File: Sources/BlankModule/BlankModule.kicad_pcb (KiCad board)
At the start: 2 copper layers, 31 x 22 mm, 2 parts

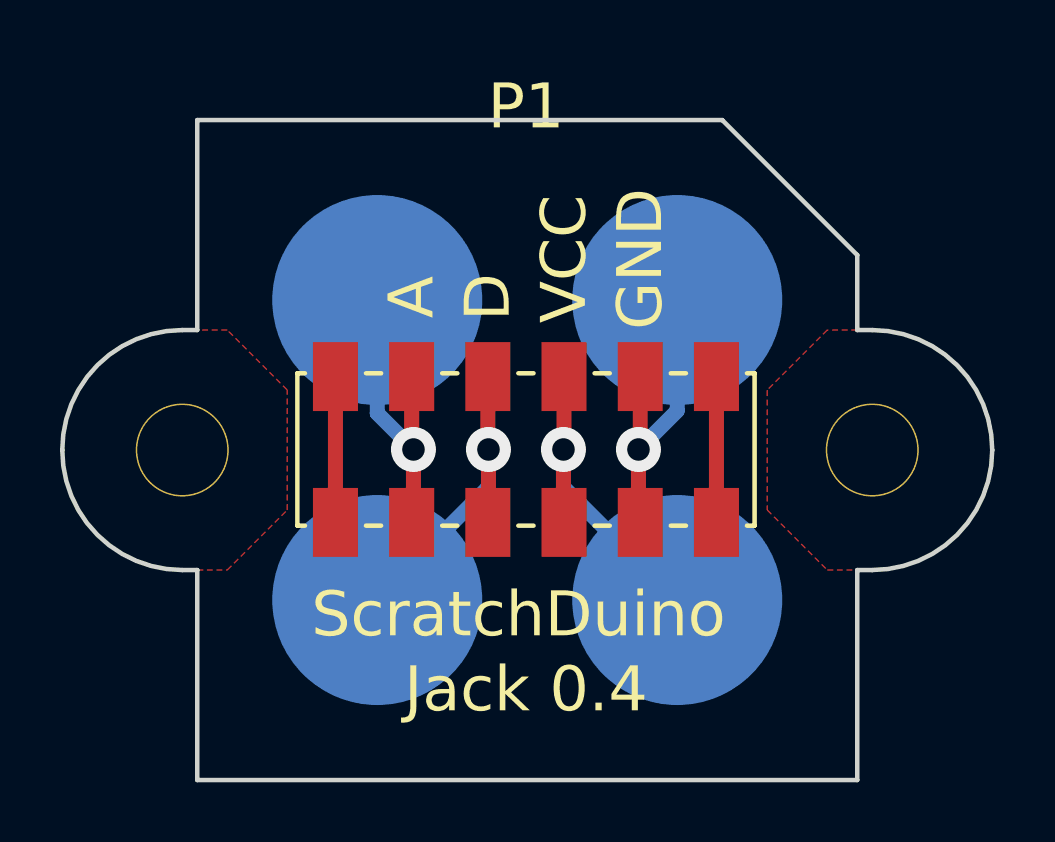
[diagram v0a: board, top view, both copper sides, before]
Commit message: Body has been added
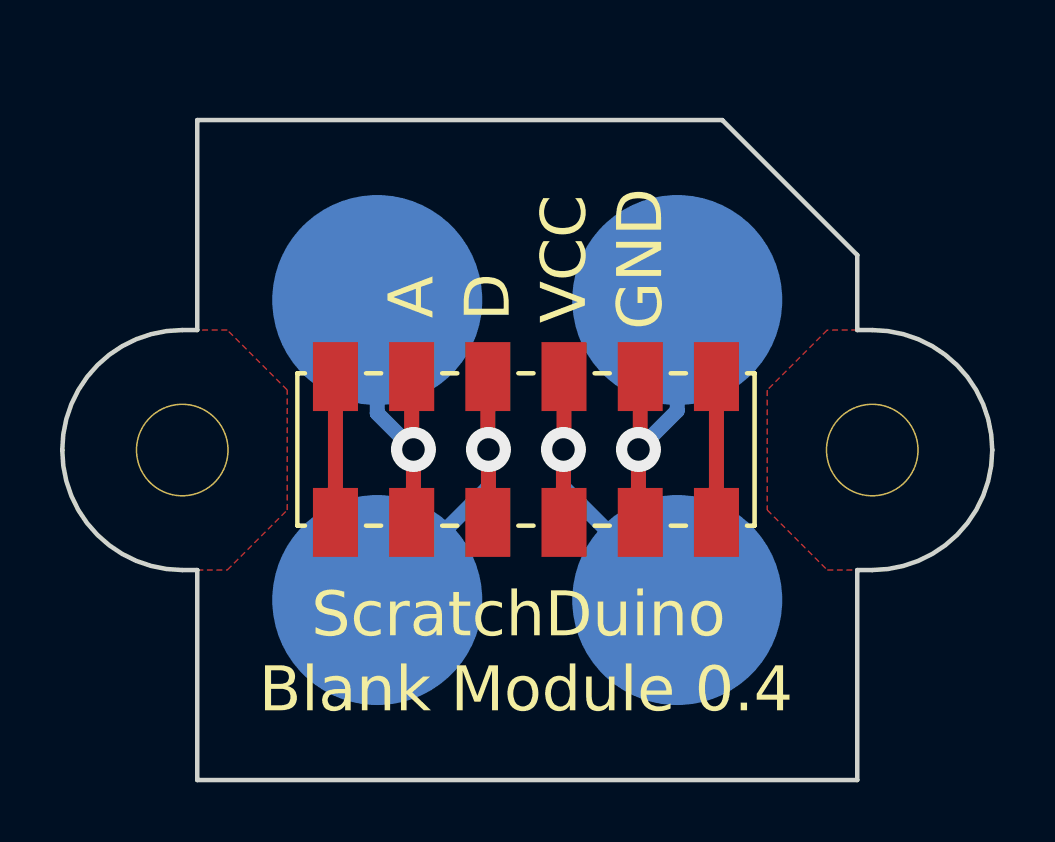
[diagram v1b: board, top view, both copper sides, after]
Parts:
- renumbered P1 to ?
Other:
- board text added: "Blank Module 0.4"
- board text removed: "Jack 0.4"
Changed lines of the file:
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@@
   (layers
     (15 F.Cu signal)
-    (0 B.Cu signal)
+    (0 B.Cu signal hide)
     (16 B.Adhes user hide)
     (17 F.Adhes user hide)
-    (18 B.Paste user)
-    (19 F.Paste user)
-    (20 B.SilkS user)
+    (18 B.Paste user hide)
+    (19 F.Paste user hide)
+    (20 B.SilkS user hide)
     (21 F.SilkS user)
     (22 B.Mask user hide)
-    (23 F.Mask user)
+    (23 F.Mask user hide)
     (24 Dwgs.User user hide)
     (25 Cmts.User user hide)
@@
   (module SENSOR_JACK (layer F.Cu)
     (at 29.25 25.75)
-    (fp_text reference P1 (at 0 -11.43) (layer F.SilkS)
+    (fp_text reference "" (at 0 -11.43) (layer F.SilkS)
       (effects (font (size 1.5 1.5) (thickness 0.15)))
     )
@@
     )
   )
-  (gr_text "Jack 0.4" (at 29.25 33.75) (layer F.SilkS)
+  (gr_text "Blank Module 0.4" (at 29.25 33.75) (layer F.SilkS)
     (effects (font (size 1.5 1.5) (thickness 0.3)))
   )
@@
   (via (at 33 25.75) (size 1.5) (layers F.Cu B.Cu) (net 1))
   (segment (start 34.293 24.457) (end 33 25.75) (width 0.5) (layer B.Cu) (net 1))
-  (segment (start 35.6 23.32) (end 35.6 28.18) (width 0.5) (layer F.Cu) (net 2) (status C00000))
-  (segment (start 22.9 23.32) (end 22.9 28.18) (width 0.5) (layer F.Cu) (net 3) (status C00000))
-  (segment (start 30.5 25.75) (end 30.5 28.16) (width 0.5) (layer F.Cu) (net 4) (status 800000))
-  (segment (start 30.5 28.16) (end 30.52 28.18) (width 0.5) (layer F.Cu) (net 4) (status C00000))
-  (segment (start 30.52 23.32) (end 30.52 25.73) (width 0.5) (layer F.Cu) (net 4) (status 400000))
-  (segment (start 34.269 30.769) (end 34.293 30.769) (width 0.5) (layer B.Cu) (net 4) (status C00000))
-  (segment (start 30.5 27) (end 34.269 30.769) (width 0.5) (layer B.Cu) (net 4) (status 800000))
+  (segment (start 35.6 23.32) (end 35.6 28.18) (width 0.5) (layer F.Cu) (net 2))
+  (segment (start 22.9 23.32) (end 22.9 28.18) (width 0.5) (layer F.Cu) (net 3))
+  (segment (start 30.5 25.75) (end 30.5 28.16) (width 0.5) (layer F.Cu) (net 4))
+  (segment (start 30.5 28.16) (end 30.52 28.18) (width 0.5) (layer F.Cu) (net 4))
+  (segment (start 30.52 23.32) (end 30.52 25.73) (width 0.5) (layer F.Cu) (net 4))
+  (segment (start 34.269 30.769) (end 34.293 30.769) (width 0.5) (layer B.Cu) (net 4))
+  (segment (start 30.5 27) (end 34.269 30.769) (width 0.5) (layer B.Cu) (net 4))
   (segment (start 30.5 25.75) (end 30.5 27) (width 0.5) (layer B.Cu) (net 4))
   (via (at 30.5 25.75) (size 1.5) (layers F.Cu B.Cu) (net 4))
   (segment (start 30.52 25.73) (end 30.5 25.75) (width 0.5) (layer F.Cu) (net 4))
-  (segment (start 28 25.75) (end 28 28.16) (width 0.5) (layer F.Cu) (net 5) (status 800000))
-  (segment (start 28 28.16) (end 27.98 28.18) (width 0.5) (layer F.Cu) (net 5) (status C00000))
-  (segment (start 27.98 23.32) (end 27.98 25.73) (width 0.5) (layer F.Cu) (net 5) (status 400000))
-  (segment (start 24.293 30.707) (end 24.293 30.769) (width 0.5) (layer B.Cu) (net 5) (status C00000))
-  (segment (start 28 27) (end 24.293 30.707) (width 0.5) (layer B.Cu) (net 5) (status 800000))
+  (segment (start 28 25.75) (end 28 28.16) (width 0.5) (layer F.Cu) (net 5))
+  (segment (start 28 28.16) (end 27.98 28.18) (width 0.5) (layer F.Cu) (net 5))
+  (segment (start 27.98 23.32) (end 27.98 25.73) (width 0.5) (layer F.Cu) (net 5))
+  (segment (start 24.293 30.707) (end 24.293 30.769) (width 0.5) (layer B.Cu) (net 5))
+  (segment (start 28 27) (end 24.293 30.707) (width 0.5) (layer B.Cu) (net 5))
   (segment (start 28 25.75) (end 28 27) (width 0.5) (layer B.Cu) (net 5))
   (via (at 28 25.75) (size 1.5) (layers F.Cu B.Cu) (net 5))
